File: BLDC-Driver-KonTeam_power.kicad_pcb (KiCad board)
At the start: 2 copper layers, 180 x 100 mm, 94 parts, among them J1 A, J2 B, J3 Logic_Conn, J4 C, J5 Logic_Test, J6 IN, Q1 IRFB3607, Q10 2N7000, Q11 2N7000, Q12 2N7000, Q2 IRFB3607, Q3 IRFB3607, Q4 IRFB3607, Q5 IRFB3607, Q6 IRFB3607, Q7 2N7000, Q8 2N7000, Q9 2N7000, U1 LM7805_TO220, U2 Buck Converter, U3 L6387, U4 L6387, U5 L6387

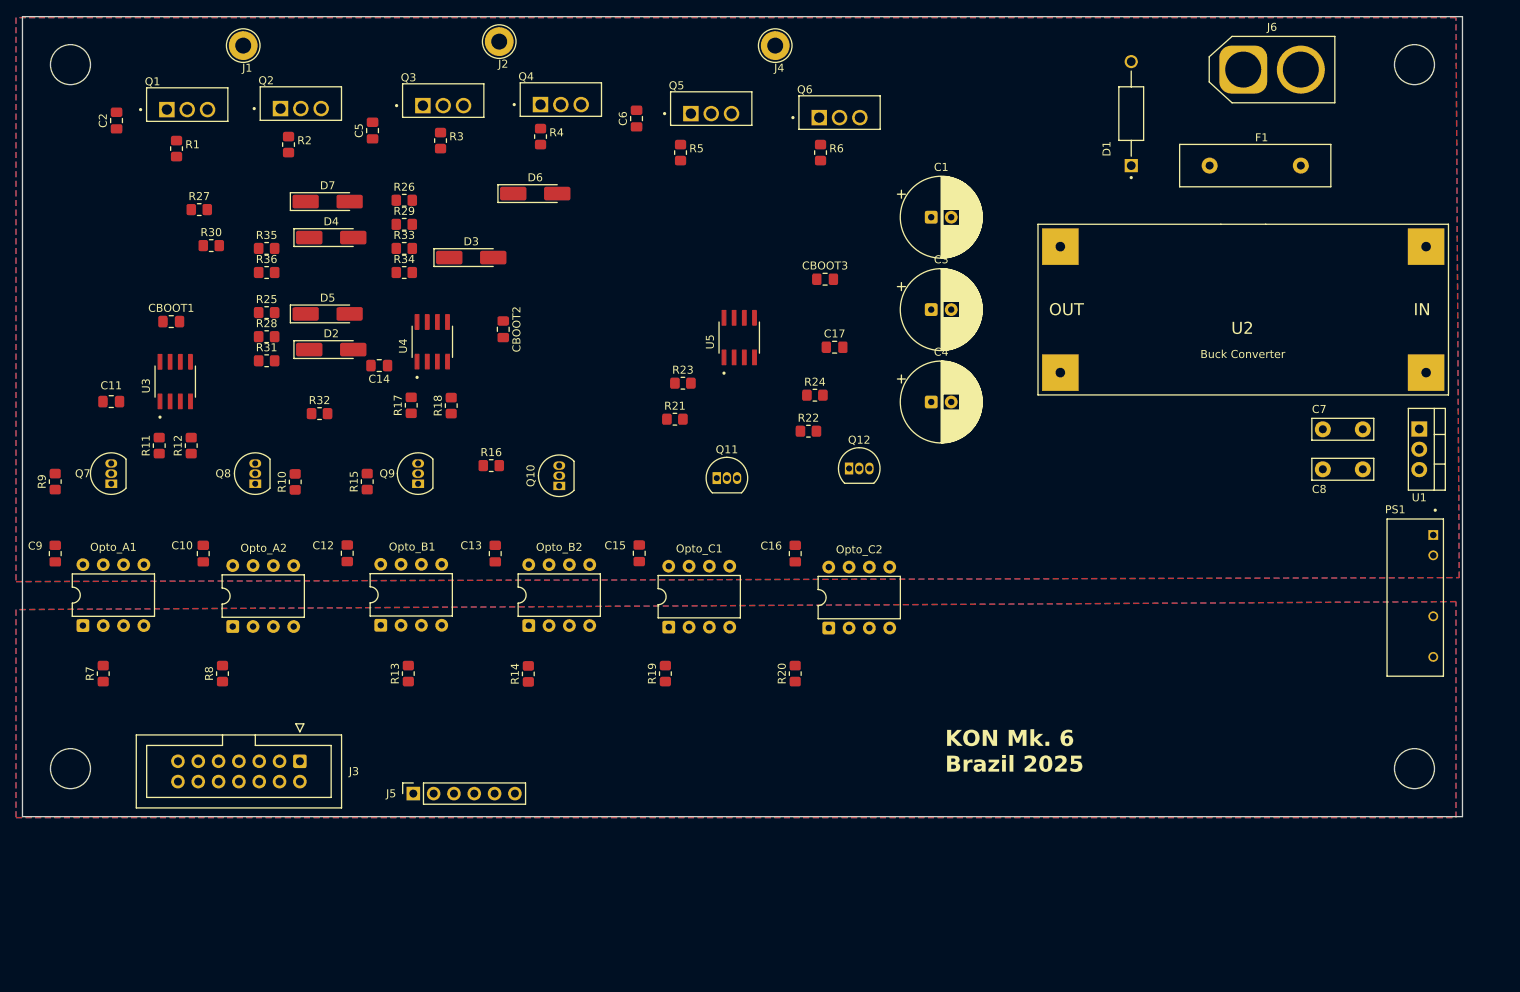
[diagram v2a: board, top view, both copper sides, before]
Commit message: posicion de las resistencias de gate corregidas
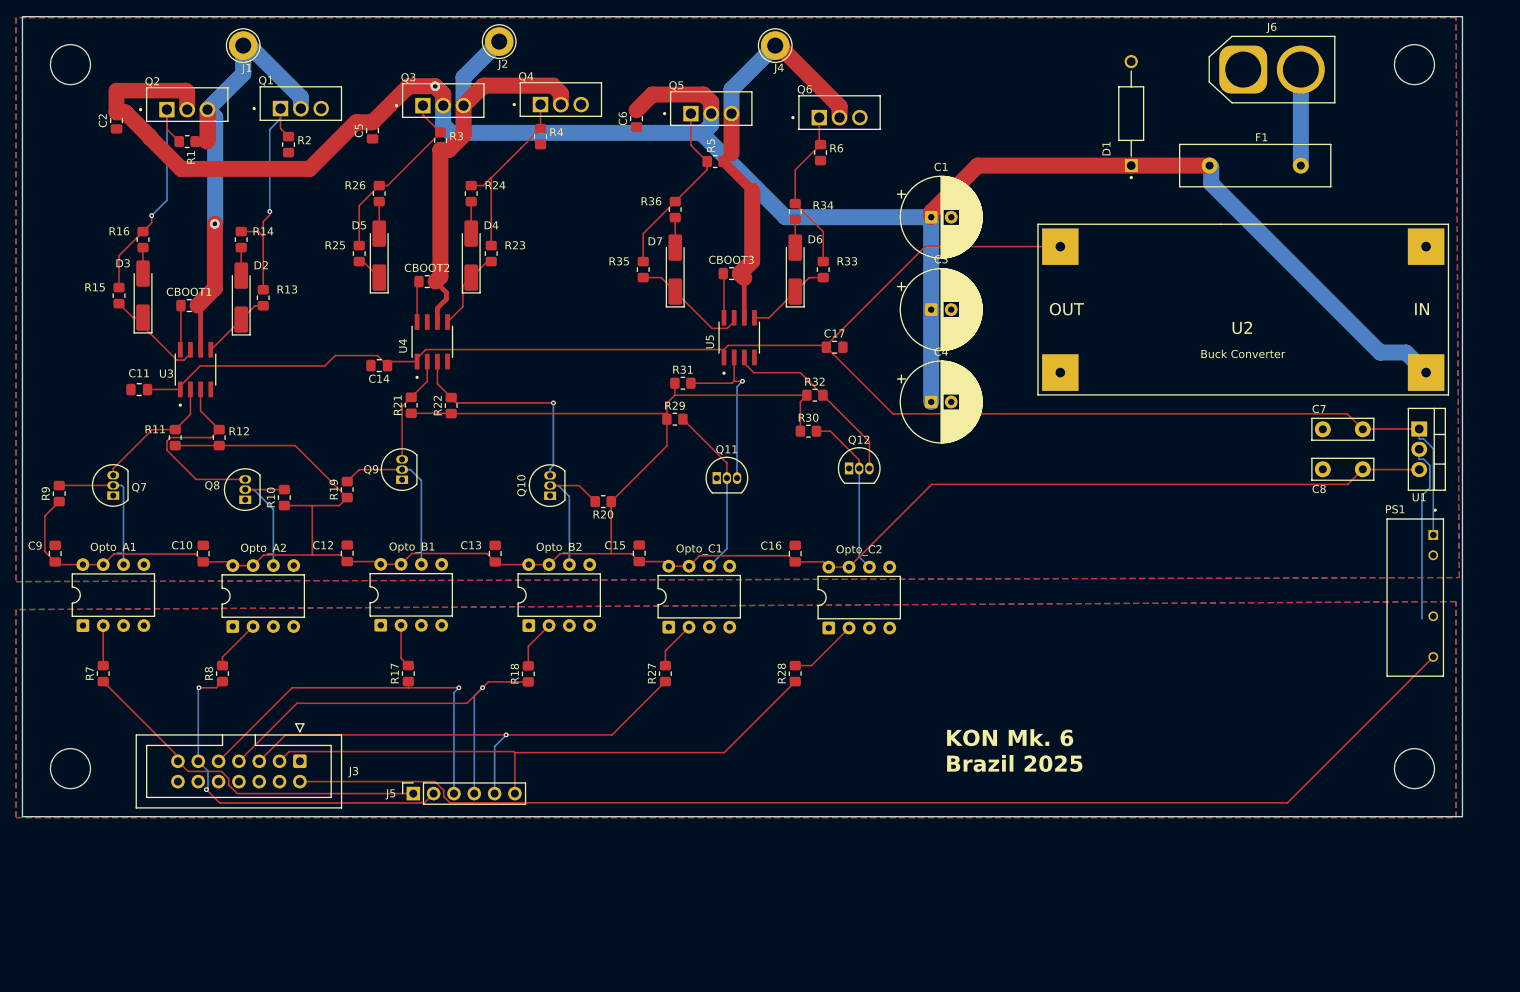
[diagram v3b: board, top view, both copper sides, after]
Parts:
- moved R33 76.6 mm to (145.0, 57.0), turned to 90 degrees
- moved R34 74.5 mm to (141.5, 49.8), turned to 90 degrees
- moved D6 58.1 mm to (141.5, 57.0), turned to 90 degrees
- moved R36 51.7 mm to (126.5, 49.5), turned to 90 degrees
- moved R35 47.1 mm to (122.5, 57.0), turned to 90 degrees
- moved D7 44.3 mm to (126.5, 57.0), turned to 90 degrees
- moved R16 31.0 mm to (60.0, 53.2), turned to 90 degrees
- moved D3 23.2 mm to (60.0, 60.2), turned to 90 degrees
- moved D5 21.0 mm to (89.5, 55.2), turned to 90 degrees
- moved R15 20.2 mm to (57.0, 60.2), turned to 90 degrees
- moved R20 14.7 mm to (117.5, 86.0), turned to 180 degrees
- moved D2 13.0 mm to (72.2, 60.5), turned to 90 degrees
- moved CBOOT3 11.7 mm to (133.5, 57.5)
- moved R23 11.5 mm to (103.5, 55.0), turned to 90 degrees
- moved CBOOT2 11.2 mm to (95.5, 58.5), turned to 0 degrees
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- renumbered D5 to D3, D3 to D4, D6 to D5, D4 to D6, Q2 to Q1, Q1 to Q2, R28 to R13, R25 to R14, R31 to R15, R32 to R16, R13 to R17, R14 to R18, R15 to R19, R16 to R20, R17 to R21, R18 to R22, R29 to R23, R26 to R24, R33 to R25, R34 to R26, R19 to R27, R20 to R28, R21 to R29, R22 to R30, R23 to R31, R24 to R32, R30 to R33, R27 to R34
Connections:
- D2 pad 1: /DriverA/Power_Low -> Net-(D2-K)
- D3 pad 1: /DriverA/Power_High -> Net-(D3-K)
- D4 pad 1: /DriverB/Power_Low -> Net-(D4-K)
- D5 pad 1: /DriverB/Power_High -> Net-(D5-K)
- D6 pad 1: /DriverC/Power_Low -> Net-(D6-K)
- D7 pad 1: /DriverC/Power_High -> Net-(D7-K)
- R13 pad 1: /DriverA/Power_Low -> Net-(D2-K)
- R13 pad 2: Net-(U3-LIN) -> LO_A
- R14 pad 2: Net-(U3-LIN) -> LO_A
- R15 pad 1: /DriverA/Power_High -> Net-(D3-K)
- R15 pad 2: Net-(U3-HIN) -> HO_A
- R16 pad 2: Net-(U3-HIN) -> HO_A
- R23 pad 1: /DriverB/Power_Low -> Net-(D4-K)
- R23 pad 2: Net-(U4-LIN) -> LO_B
- R24 pad 2: Net-(U4-LIN) -> LO_B
- R25 pad 1: /DriverB/Power_High -> Net-(D5-K)
- R25 pad 2: Net-(U4-HIN) -> HO_B
- R26 pad 2: Net-(U4-HIN) -> HO_B
- R33 pad 1: /DriverC/Power_Low -> Net-(D6-K)
- R33 pad 2: Net-(U5-LIN) -> LO_C
- R34 pad 2: Net-(U5-LIN) -> LO_C
- R35 pad 1: /DriverC/Power_High -> Net-(D7-K)
- R35 pad 2: Net-(U5-HIN) -> HO_C
- R36 pad 2: Net-(U5-HIN) -> HO_C
- U3 pad 2: Net-(U3-HIN) -> /DriverA/Power_High
- U3 pad 3: Net-(U3-LIN) -> /DriverA/Power_Low
- U3 pad 5: LO_A -> Net-(D2-K)
- U3 pad 7: HO_A -> Net-(D3-K)
- U4 pad 2: Net-(U4-HIN) -> /DriverB/Power_High
- U4 pad 3: Net-(U4-LIN) -> /DriverB/Power_Low
- U4 pad 5: LO_B -> Net-(D4-K)
- U4 pad 7: HO_B -> Net-(D5-K)
- U5 pad 2: Net-(U5-HIN) -> /DriverC/Power_High
- U5 pad 3: Net-(U5-LIN) -> /DriverC/Power_Low
- U5 pad 5: LO_C -> Net-(D6-K)
- U5 pad 7: HO_C -> Net-(D7-K)
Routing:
- net +5V: track 0.00 -> 306.8 mm
- net VCC: track 0.00 -> 249.6 mm, vias 0 -> 1
- net +12V: track 0.00 -> 216.9 mm
- net +5VL: track 0.00 -> 150.8 mm
- net LIN_C: track 0.00 -> 73.8 mm
- net HIN_C: track 0.00 -> 62.8 mm, vias 0 -> 1
- net MA: track 0.00 -> 57.9 mm, vias 0 -> 1
- net MB: track 0.00 -> 55.2 mm
- net LIN_B: track 0.00 -> 53.9 mm, vias 0 -> 1
- net MC: track 0.00 -> 51.7 mm
- net HIN_B: track 0.00 -> 48.1 mm, vias 0 -> 1
- net LIN_A: track 0.00 -> 46.2 mm, vias 0 -> 2
- net HIN_A: track 0.00 -> 45.4 mm
- net LO_A: track 0.00 -> 30.4 mm, vias 0 -> 1
- net HO_A: track 0.00 -> 29.4 mm, vias 0 -> 1
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
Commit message: correciones( aislamiento LM7805) , cambio de ID , primer ruteo
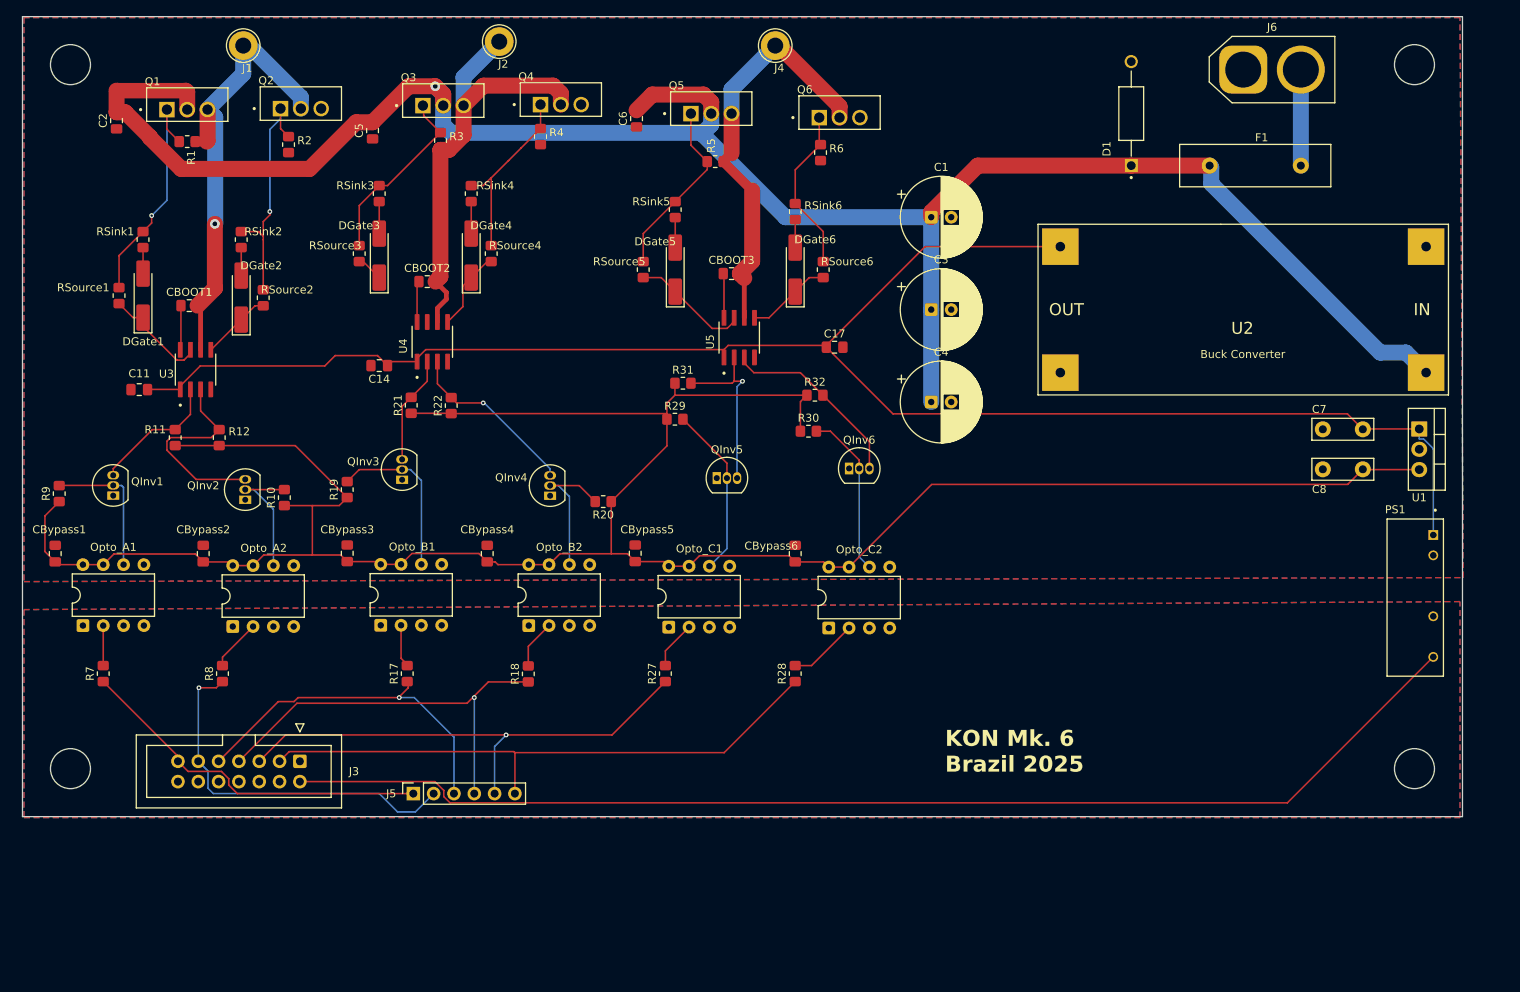
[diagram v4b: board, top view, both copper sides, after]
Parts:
- moved CBypass4 1.00 mm to (103.0, 92.5)
- moved CBypass5 0.50 mm to (121.5, 92.5)
- moved R17 0.13 mm to (93.0, 107.5)
- renumbered C9 to CBypass1, C10 to CBypass2, C12 to CBypass3, C13 to CBypass4, C15 to CBypass5, C16 to CBypass6, D3 to DGate1, D2 to DGate2, D5 to DGate3, D4 to DGate4, D7 to DGate5, D6 to DGate6, Q2 to Q1, Q1 to Q2, Q7 to QInv1, Q8 to QInv2, Q9 to QInv3, Q10 to QInv4, Q11 to QInv5, Q12 to QInv6, R16 to RSink1, R14 to RSink2, R26 to RSink3, R24 to RSink4, R36 to RSink5, R34 to RSink6, R15 to RSource1, R13 to RSource2, R25 to RSource3, R23 to RSource4, R35 to RSource5, R33 to RSource6
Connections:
- U1 pad 2: Earth -> GND
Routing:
- net Earth: track 22.5 -> 0.00 mm
- net /DriverB/Power_Low: track 27.5 -> 22.1 mm
- net HIN_B: track 48.1 -> 44.3 mm
- net LIN_B: track 53.9 -> 52.4 mm
- net LIN_A: track 46.2 -> 46.7 mm, vias 2 -> 1
